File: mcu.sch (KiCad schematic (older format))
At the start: 61 parts, among them J10 JTAG, J2 SPI1, J3 uSD, J4 I2C1, J5 serial1, J6 serial2, J7 touch interface, J8 LCD 4.3, J9 EXT_IOS, SW1 reset, U3 AT25SF641, U5 STM32F750Z8, U6 MP3302DJ-LF-P, U7 ESP32-WROOM-32, Y1 25 MHz, Y2 32.768 kHz

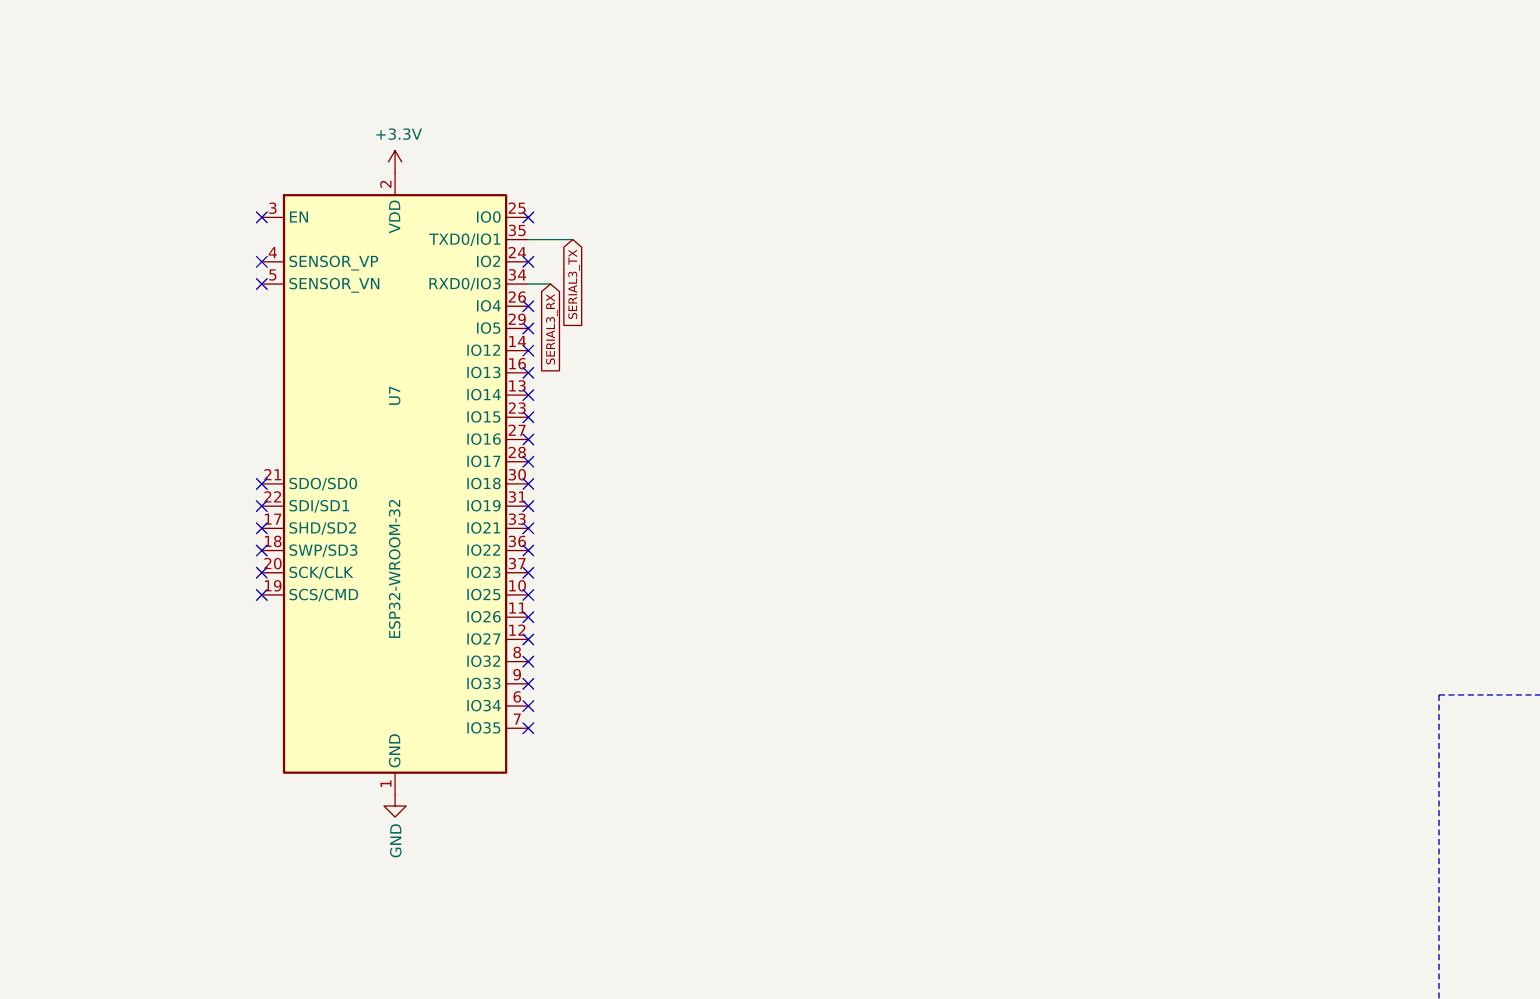
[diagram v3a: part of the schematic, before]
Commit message: add esp32 headers
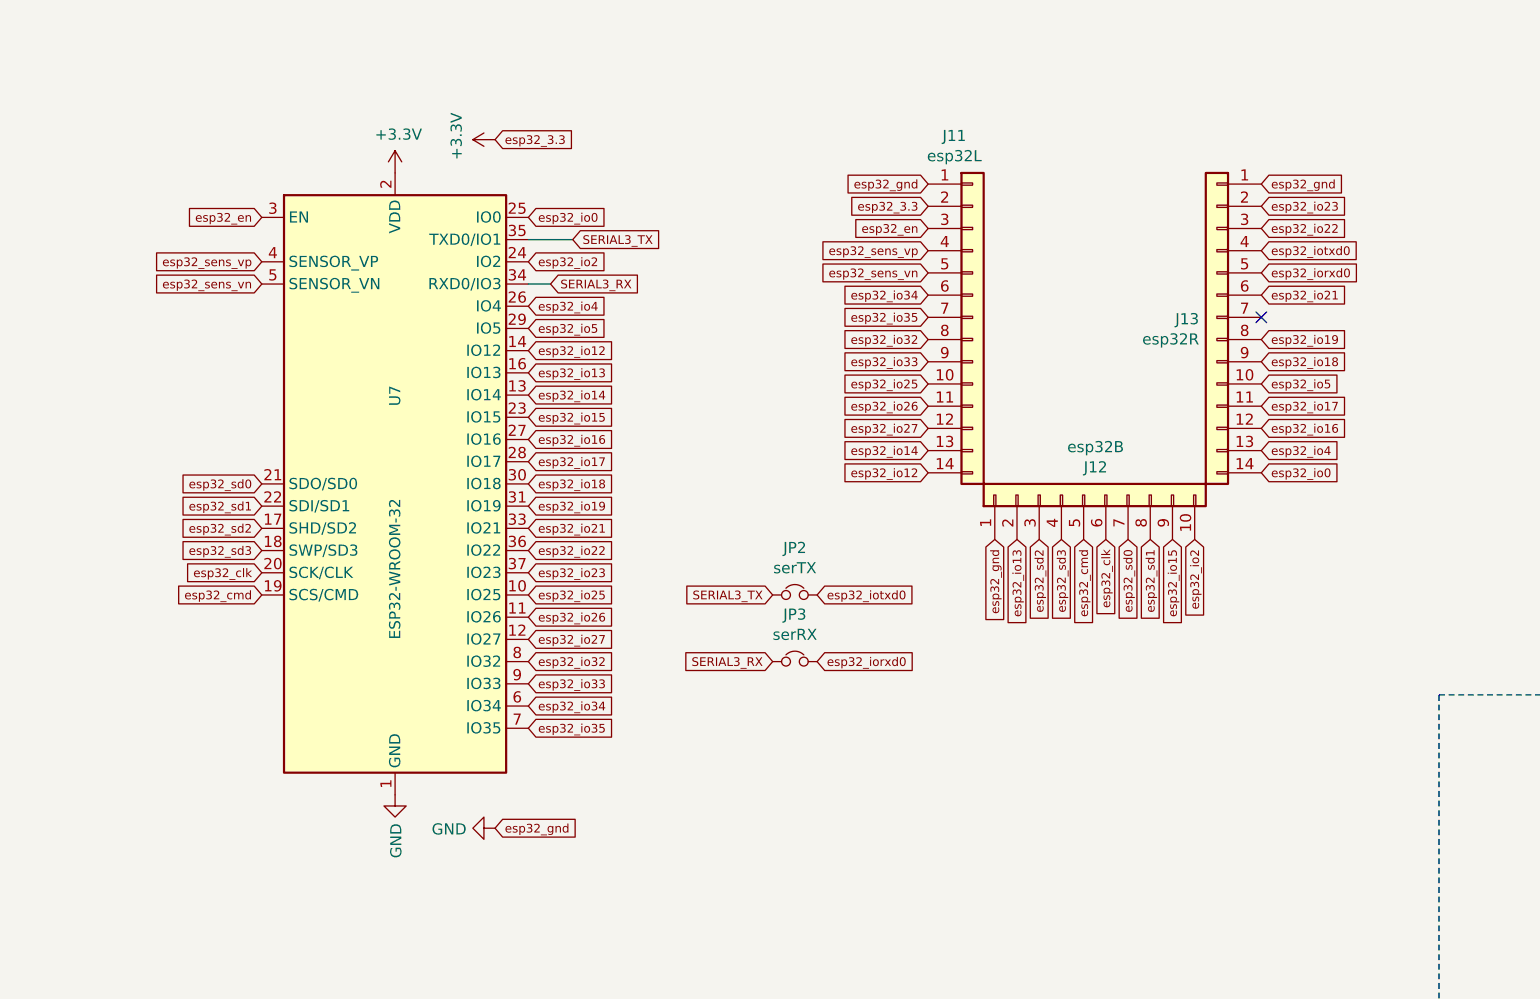
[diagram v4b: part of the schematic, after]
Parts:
- added J11: esp32L, symbol Connector_Generic:Conn_01x14
- added J12: esp32B, symbol Connector_Generic:Conn_01x10
- added J13: esp32R, symbol Connector_Generic:Conn_01x14
- added JP2: serTX, symbol Device:Jumper_NC_Small
- added JP3: serRX, symbol Device:Jumper_NC_Small
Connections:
- net +3V3: now also J11.2 (Pin_2)
- net GND: now also J11.1 (Pin_1), J12.1 (Pin_1), J13.1 (Pin_1)
- net SERIAL3_RX: now also JP3.1
- net SERIAL3_TX: now also JP2.1
- net esp32_io25: now reaches U7.10 (IO25)
- net esp32_io25: now also J11.10 (Pin_10)
- net esp32_io26: now reaches U7.11 (IO26)
- net esp32_io26: now also J11.11 (Pin_11)
- net esp32_io27: now reaches U7.12 (IO27)
- net esp32_io27: now also J11.12 (Pin_12)
- net esp32_io14: now reaches U7.13 (IO14)
- net esp32_io14: now also J11.13 (Pin_13)
- net esp32_io12: now reaches U7.14 (IO12)
- net esp32_io12: now also J11.14 (Pin_14)
- net esp32_io13: now reaches U7.16 (IO13)
- net esp32_io13: now also J12.2 (Pin_2)
- net esp32_sd2: now reaches U7.17 (SHD/SD2)
- net esp32_sd2: now also J12.3 (Pin_3)
- net esp32_sd3: now reaches U7.18 (SWP/SD3)
- net esp32_sd3: now also J12.4 (Pin_4)
- net esp32_cmd: now reaches U7.19 (SCS/CMD)
- net esp32_cmd: now also J12.5 (Pin_5)
- net esp32_clk: now reaches U7.20 (SCK/CLK)
- net esp32_clk: now also J12.6 (Pin_6)
- net esp32_sd0: now reaches U7.21 (SDO/SD0)
- net esp32_sd0: now also J12.7 (Pin_7)
- net esp32_sd1: now reaches U7.22 (SDI/SD1)
- net esp32_sd1: now also J12.8 (Pin_8)
- net esp32_io15: now reaches U7.23 (IO15)
- net esp32_io15: now also J12.9 (Pin_9)
- net esp32_io2: now reaches U7.24 (IO2)
- net esp32_io2: now also J12.10 (Pin_10)
- net esp32_io0: now reaches U7.25 (IO0)
- net esp32_io0: now also J13.14 (Pin_14)
- net esp32_io4: now reaches U7.26 (IO4)
- net esp32_io4: now also J13.13 (Pin_13)
- net esp32_io16: now reaches U7.27 (IO16)
- net esp32_io16: now also J13.12 (Pin_12)
- net esp32_io17: now reaches U7.28 (IO17)
- net esp32_io17: now also J13.11 (Pin_11)
- net esp32_io5: now reaches U7.29 (IO5)
- net esp32_io5: now also J13.10 (Pin_10)
- net esp32_en: now reaches U7.3 (EN)
- net esp32_en: now also J11.3 (Pin_3)
- net esp32_io18: now reaches U7.30 (IO18)
- net esp32_io18: now also J13.9 (Pin_9)
- net esp32_io19: now reaches U7.31 (IO19)
- net esp32_io19: now also J13.8 (Pin_8)
- net esp32_io21: now reaches U7.33 (IO21)
- net esp32_io21: now also J13.6 (Pin_6)
- net esp32_io22: now reaches U7.36 (IO22)
- net esp32_io22: now also J13.3 (Pin_3)
- net esp32_io23: now reaches U7.37 (IO23)
- net esp32_io23: now also J13.2 (Pin_2)
- net esp32_sens_vp: now reaches U7.4 (SENSOR_VP)
- net esp32_sens_vp: now also J11.4 (Pin_4)
- net esp32_sens_vn: now reaches U7.5 (SENSOR_VN)
- net esp32_sens_vn: now also J11.5 (Pin_5)
- net esp32_io34: now reaches U7.6 (IO34)
- net esp32_io34: now also J11.6 (Pin_6)
- net esp32_io35: now reaches U7.7 (IO35)
- net esp32_io35: now also J11.7 (Pin_7)
- net esp32_io32: now reaches U7.8 (IO32)
- net esp32_io32: now also J11.8 (Pin_8)
- net esp32_io33: now reaches U7.9 (IO33)
- net esp32_io33: now also J11.9 (Pin_9)
- new net esp32_iorxd0: J13.5 (Pin_5), JP3.2
- new net esp32_iotxd0: J13.4 (Pin_4), JP2.2
- no-connect marks 45 -> 15

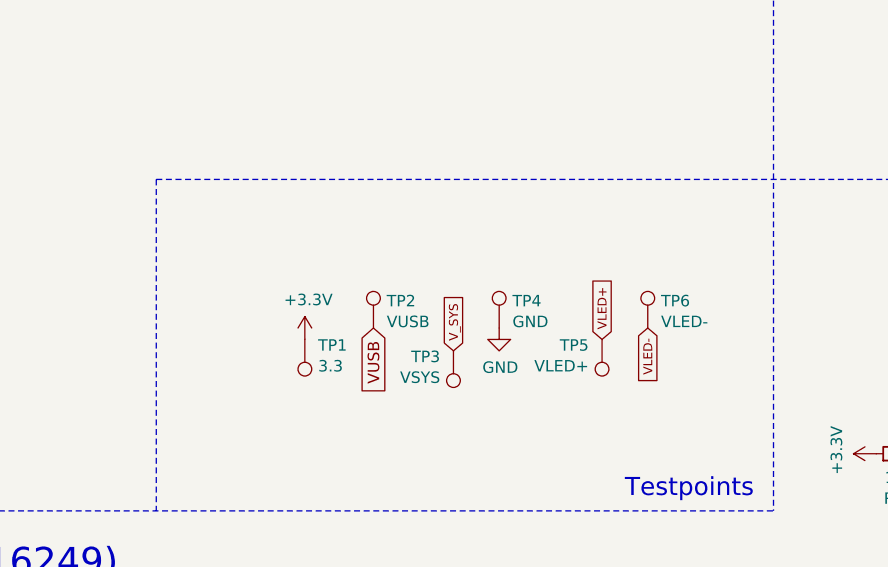
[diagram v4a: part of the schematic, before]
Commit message: Add TPs
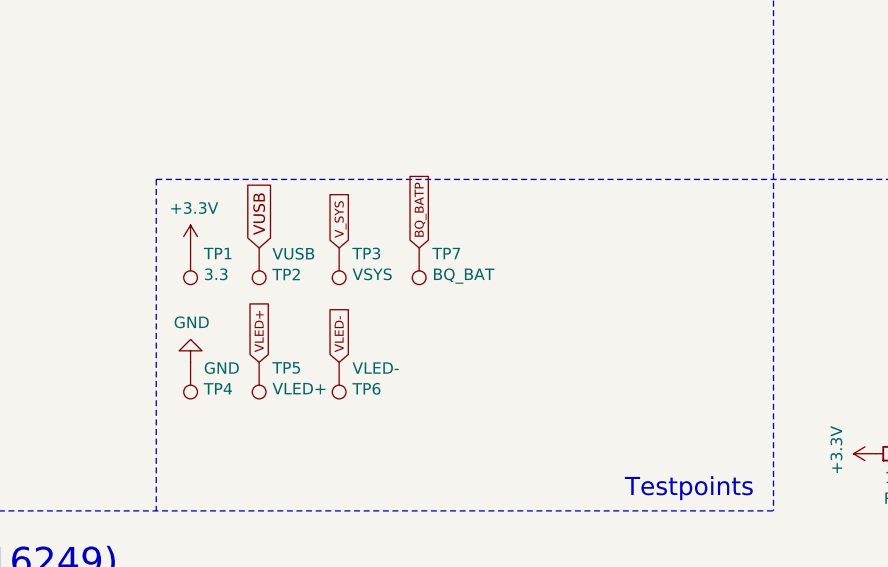
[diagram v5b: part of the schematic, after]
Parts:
- added TP7: BQ_BAT, symbol Connector:TestPoint
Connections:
- new net BQ_BATP: TP7.1
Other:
- moved on the sheet: TP1, TP2, TP3, TP4, TP5, TP6
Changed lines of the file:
@@
 L Connector:TestPoint TP1
 U 1 1 60C6D521
-P 7550 4250
-F 0 "TP1" H 7492 4276 50  0000 R CNN
-F 1 "3.3" H 7492 4367 50  0000 R CNN
-F 2 "" H 7750 4250 50  0001 C CNN
-F 3 "~" H 7750 4250 50  0001 C CNN
-	1    7550 4250
+P 7050 3850
+F 0 "TP1" H 6992 3876 50  0000 R CNN
+F 1 "3.3" H 6992 3967 50  0000 R CNN
+F 2 "" H 7250 3850 50  0001 C CNN
+F 3 "~" H 7250 3850 50  0001 C CNN
+	1    7050 3850
 	-1   0    0    1
 $EndComp
@@
 L Connector:TestPoint TP2
 U 1 1 60C6DC35
-P 7850 4200
-F 0 "TP2" H 7908 4318 50  0000 L CNN
-F 1 "VUSB" H 7908 4227 50  0000 L CNN
-F 2 "" H 8050 4200 50  0001 C CNN
-F 3 "~" H 8050 4200 50  0001 C CNN
-	1    7850 4200
-	1    0    0    -1
-$EndComp
-Text GLabel 7850 4200 3    50   Input ~ 0
+P 7350 3850
+F 0 "TP2" H 7408 3968 50  0000 L CNN
+F 1 "VUSB" H 7408 3877 50  0000 L CNN
+F 2 "" H 7550 3850 50  0001 C CNN
+F 3 "~" H 7550 3850 50  0001 C CNN
+	1    7350 3850
+	1    0    0    1
+$EndComp
+Text GLabel 7350 3850 1    50   Input ~ 0
 VUSB
 $Comp
 L Connector:TestPoint TP3
 U 1 1 60C6EE25
-P 8200 4300
-F 0 "TP3" H 8142 4326 50  0000 R CNN
-F 1 "VSYS" H 8142 4417 50  0000 R CNN
-F 2 "" H 8400 4300 50  0001 C CNN
-F 3 "~" H 8400 4300 50  0001 C CNN
-	1    8200 4300
-	1    0    0    1
-$EndComp
-Text GLabel 8200 4300 1    39   Input ~ 0
+P 7700 3850
+F 0 "TP3" H 7642 3876 50  0000 R CNN
+F 1 "VSYS" H 7642 3967 50  0000 R CNN
+F 2 "" H 7900 3850 50  0001 C CNN
+F 3 "~" H 7900 3850 50  0001 C CNN
+	1    7700 3850
+	-1   0    0    1
+$EndComp
+Text GLabel 7700 3850 1    39   Input ~ 0
 V_SYS
 $Comp
 L power:+3.3V #PWR08
 U 1 1 60C70150
-P 7550 4250
-F 0 "#PWR08" H 7550 4100 50  0001 C CNN
-F 1 "+3.3V" H 7565 4423 50  0000 C CNN
-F 2 "" H 7550 4250 50  0001 C CNN
-F 3 "" H 7550 4250 50  0001 C CNN
-	1    7550 4250
+P 7050 3850
+F 0 "#PWR08" H 7050 3700 50  0001 C CNN
+F 1 "+3.3V" H 7065 4023 50  0000 C CNN
+F 2 "" H 7050 3850 50  0001 C CNN
+F 3 "" H 7050 3850 50  0001 C CNN
+	1    7050 3850
 	1    0    0    -1
 $EndComp
@@
 L Connector:TestPoint TP4
 U 1 1 60CDAE0F
-P 8400 4200
-F 0 "TP4" H 8458 4318 50  0000 L CNN
-F 1 "GND" H 8458 4227 50  0000 L CNN
-F 2 "" H 8600 4200 50  0001 C CNN
-F 3 "~" H 8600 4200 50  0001 C CNN
-	1    8400 4200
-	1    0    0    -1
+P 7050 4350
+F 0 "TP4" H 7108 4468 50  0000 L CNN
+F 1 "GND" H 7108 4377 50  0000 L CNN
+F 2 "" H 7250 4350 50  0001 C CNN
+F 3 "~" H 7250 4350 50  0001 C CNN
+	1    7050 4350
+	1    0    0    1
 $EndComp
 $Comp
 L power:GND #PWR010
 U 1 1 60CDB10D
-P 8400 4200
-F 0 "#PWR010" H 8400 3950 50  0001 C CNN
-F 1 "GND" H 8405 4027 50  0000 C CNN
-F 2 "" H 8400 4200 50  0001 C CNN
-F 3 "" H 8400 4200 50  0001 C CNN
-	1    8400 4200
-	1    0    0    -1
+P 7050 4350
+F 0 "#PWR010" H 7050 4100 50  0001 C CNN
+F 1 "GND" H 7055 4177 50  0000 C CNN
+F 2 "" H 7050 4350 50  0001 C CNN
+F 3 "" H 7050 4350 50  0001 C CNN
+	1    7050 4350
+	1    0    0    1
 $EndComp
 Text Notes 8950 4950 0    79   ~ 0
@@
 L Connector:TestPoint TP6
 U 1 1 60CE0C95
-P 9050 4200
-F 0 "TP6" H 9108 4318 50  0000 L CNN
-F 1 "VLED-" H 9108 4227 50  0000 L CNN
-F 2 "" H 9250 4200 50  0001 C CNN
-F 3 "~" H 9250 4200 50  0001 C CNN
-	1    9050 4200
-	1    0    0    -1
+P 7700 4350
+F 0 "TP6" H 7758 4468 50  0000 L CNN
+F 1 "VLED-" H 7758 4377 50  0000 L CNN
+F 2 "" H 7900 4350 50  0001 C CNN
+F 3 "~" H 7900 4350 50  0001 C CNN
+	1    7700 4350
+	1    0    0    1
 $EndComp
 $Comp
 L Connector:TestPoint TP5
 U 1 1 60CE10AB
-P 8850 4250
-F 0 "TP5" H 8792 4276 50  0000 R CNN
-F 1 "VLED+" H 8792 4367 50  0000 R CNN
-F 2 "" H 9050 4250 50  0001 C CNN
-F 3 "~" H 9050 4250 50  0001 C CNN
-	1    8850 4250
-	1    0    0    1
-$EndComp
-Text GLabel 8850 4250 1    39   Input ~ 0
+P 7350 4350
+F 0 "TP5" H 7292 4376 50  0000 R CNN
+F 1 "VLED+" H 7292 4467 50  0000 R CNN
+F 2 "" H 7550 4350 50  0001 C CNN
+F 3 "~" H 7550 4350 50  0001 C CNN
+	1    7350 4350
+	-1   0    0    1
+$EndComp
+Text GLabel 7350 4350 1    39   Input ~ 0
 VLED+
-Text GLabel 9050 4200 3    39   Input ~ 0
+Text GLabel 7700 4350 1    39   Input ~ 0
 VLED-
 Wire Notes Line
@@
 Text GLabel 1600 3100 0    39   Input ~ 0
 esp32_cmd
+Text GLabel 8050 3850 1    39   Input ~ 0
+BQ_BATP
+$Comp
+L Connector:TestPoint TP7
+U 1 1 60FE1681
+P 8050 3850
+F 0 "TP7" H 7992 3876 50  0000 R CNN
+F 1 "BQ_BAT" H 7992 3967 50  0000 R CNN
+F 2 "" H 8250 3850 50  0001 C CNN
+F 3 "~" H 8250 3850 50  0001 C CNN
+	1    8050 3850
+	-1   0    0    1
+$EndComp
 $EndSCHEMATC

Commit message: it is
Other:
- note added: "TODO to validate:\n- BOOT0 behavior\n- WAKEUP through ON behavior\n- RESET\n- caps for stm32 25MHz xtal"
- note removed: "TODO to validate:\n- BOOT0 behavior\n- WAKEUP through ON behavior\n- RESET\n- caps for stm32 25MHz xtal\n- if usb host, VUSB isn't powered"
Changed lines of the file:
@@
 BOOT0
 Text Notes 600  11100 0    98   ~ 0
-TODO to validate:\n- BOOT0 behavior\n- WAKEUP through ON behavior\n- RESET\n- caps for stm32 25MHz xtal\n- if usb host, VUSB isn't powered
+TODO to validate:\n- BOOT0 behavior\n- WAKEUP through ON behavior\n- RESET\n- caps for stm32 25MHz xtal
 Text GLabel 4800 9350 0    50   Input ~ 0
 KB_ROW_11

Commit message: switch to right xtals
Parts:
- removed C30: 10pF, symbol Device:C_Small
- removed Y1: 25 MHz, symbol Device:Crystal
- added R25: 10k, symbol Device:R_Small
- added R26: 100, symbol Device:R_Small
- added U8: ASDMB-25.000MHZ-LC-T, Oscillator:Oscillator_SMD_Abracon_ASDMB-4Pin_2.5x2.0mm, symbol Oscillator:ASDMB-xxxMHz
- C29: value 10pF -> 100nF
- Y2: mouser (none) -> 815-ABS0716632.768KT
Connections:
- net +3V3: now also C29.1, R25.1, U8.4 (VDD)
- net GND: now also C29.2, U8.2 (GND); no longer C29.1
- net OSC_IN: no longer names the net of U5.23 (PH0)
- net OSC_IN: now also R26.1; no longer C29.2
- net OSC_OUT: no longer names the net of U5.24 (PH1)
- new net: R25.2, U8.1 (Standby)
- new net OSC_25M: R26.2, U8.3 (Out)
- no-connect marks 15 -> 16
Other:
- note added: "ABS07-166-32.768KHZ-T"
- note added: "TODO to validate:\n- BOOT0 behavior\n- WAKEUP through ON behavior\n- RESET"
- note removed: "TODO to validate:\n- BOOT0 behavior\n- WAKEUP through ON behavior\n- RESET\n- caps for stm32 25MHz xtal"
- note removed: "xtal with\nintegrated\ncaps"
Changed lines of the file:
@@
 $EndDescr
-$Comp
-L Device:Crystal Y1
-U 1 1 5F7C8337
-P 12000 3600
-F 0 "Y1" H 12000 3868 50  0000 C CNN
-F 1 "25 MHz" H 12000 3777 50  0000 C CNN
-F 2 "" H 12000 3600 50  0001 C CNN
-F 3 "~" H 12000 3600 50  0001 C CNN
-	1    12000 3600
-	0    1    1    0
-$EndComp
 $Comp
 L Device:Crystal Y2
@@
 F 2 "" H 15950 7000 50  0001 C CNN
 F 3 "~" H 15950 7000 50  0001 C CNN
+F 4 "815-ABS0716632.768KT" H 15950 7000 50  0001 C CNN "mouser"
 	1    15950 7000
 	0    -1   -1   0
@@
 Text Label 15100 7050 0    39   ~ 0
 OSC32_OUT
-Text Notes 15650 6700 0    39   ~ 0
-xtal with\nintegrated\ncaps
-Text Label 12450 3550 0    39   ~ 0
-OSC_IN
-Text Label 12450 3650 0    39   ~ 0
-OSC_OUT
-Wire Wire Line
-	12750 3650 12300 3650
-Wire Wire Line
-	12300 3650 12300 3800
-Wire Wire Line
-	12300 3800 12000 3800
-Wire Wire Line
-	12000 3800 12000 3750
-Wire Wire Line
-	12000 3450 12000 3400
-Wire Wire Line
-	12000 3400 12300 3400
-Wire Wire Line
-	12300 3400 12300 3550
-Wire Wire Line
-	12300 3550 12750 3550
 Text GLabel 14500 1950 1    50   Input ~ 0
 VUSB
@@
 BOOT0
 Text Notes 600  11100 0    98   ~ 0
-TODO to validate:\n- BOOT0 behavior\n- WAKEUP through ON behavior\n- RESET\n- caps for stm32 25MHz xtal
+TODO to validate:\n- BOOT0 behavior\n- WAKEUP through ON behavior\n- RESET
 Text GLabel 4800 9350 0    50   Input ~ 0
 KB_ROW_11
@@
 Wire Wire Line
 	10600 1850 10900 1850
-$Comp
-L Device:C_Small C29
-U 1 1 602A0B0B
-P 11900 3400
-F 0 "C29" V 12129 3400 50  0000 C CNN
-F 1 "10pF" V 12038 3400 50  0000 C CNN
-F 2 "" H 11900 3400 50  0001 C CNN
-F 3 "~" H 11900 3400 50  0001 C CNN
-	1    11900 3400
-	0    -1   -1   0
-$EndComp
-Connection ~ 12000 3400
-$Comp
-L Device:C_Small C30
-U 1 1 602A1326
-P 11900 3800
-F 0 "C30" V 11700 3800 50  0000 C CNN
-F 1 "10pF" V 11800 3800 50  0000 C CNN
-F 2 "" H 11900 3800 50  0001 C CNN
-F 3 "~" H 11900 3800 50  0001 C CNN
-	1    11900 3800
-	0    -1   -1   0
-$EndComp
-Connection ~ 12000 3800
-$Comp
-L power:GND #PWR0140
-U 1 1 602A1994
-P 11800 3400
-F 0 "#PWR0140" H 11800 3150 50  0001 C CNN
-F 1 "GND" H 11805 3227 50  0000 C CNN
-F 2 "" H 11800 3400 50  0001 C CNN
-F 3 "" H 11800 3400 50  0001 C CNN
-	1    11800 3400
-	0    1    1    0
-$EndComp
-$Comp
-L power:GND #PWR0141
-U 1 1 602A2015
-P 11800 3800
-F 0 "#PWR0141" H 11800 3550 50  0001 C CNN
-F 1 "GND" H 11805 3627 50  0000 C CNN
-F 2 "" H 11800 3800 50  0001 C CNN
-F 3 "" H 11800 3800 50  0001 C CNN
-	1    11800 3800
-	0    1    1    0
-$EndComp
 Text Notes 11550 4200 0    39   ~ 0
 validate caps against\nchoosen xtal
@@
 	-1   0    0    1
 $EndComp
+Text Notes 15650 6700 0    39   ~ 0
+ABS07-166-32.768KHZ-T
+$Comp
+L Oscillator:ASDMB-xxxMHz U8
+U 1 1 60FEB22A
+P 10600 2950
+F 0 "U8" H 11044 2996 50  0000 L CNN
+F 1 "ASDMB-25.000MHZ-LC-T" H 10100 2500 50  0000 L CNN
+F 2 "Oscillator:Oscillator_SMD_Abracon_ASDMB-4Pin_2.5x2.0mm" H 10600 2950 50  0001 C CNN
+F 3 "https://abracon.com/Oscillators/ASDMB.pdf" H 10900 3400 50  0001 C CNN
+	1    10600 2950
+	1    0    0    -1
+$EndComp
+$Comp
+L Device:R_Small R25
+U 1 1 60FEC7BE
+P 10000 2950
+F 0 "R25" V 10196 2950 50  0000 C CNN
+F 1 "10k" V 10105 2950 50  0000 C CNN
+F 2 "" H 10000 2950 50  0001 C CNN
+F 3 "~" H 10000 2950 50  0001 C CNN
+	1    10000 2950
+	0    -1   -1   0
+$EndComp
+$Comp
+L Device:C_Small C29
+U 1 1 60FED86D
+P 9850 3150
+F 0 "C29" H 9942 3196 50  0000 L CNN
+F 1 "100nF" H 9942 3105 50  0000 L CNN
+F 2 "" H 9850 3150 50  0001 C CNN
+F 3 "~" H 9850 3150 50  0001 C CNN
+	1    9850 3150
+	1    0    0    -1
+$EndComp
+$Comp
+L power:+3.3V #PWR045
+U 1 1 60FEF86B
+P 9850 2650
+F 0 "#PWR045" H 9850 2500 50  0001 C CNN
+F 1 "+3.3V" H 9865 2823 50  0000 C CNN
+F 2 "" H 9850 2650 50  0001 C CNN
+F 3 "" H 9850 2650 50  0001 C CNN
+	1    9850 2650
+	1    0    0    -1
+$EndComp
+$Comp
+L power:GND #PWR046
+U 1 1 60FEFF10
+P 9850 3250
+F 0 "#PWR046" H 9850 3000 50  0001 C CNN
+F 1 "GND" H 9855 3077 50  0000 C CNN
+F 2 "" H 9850 3250 50  0001 C CNN
+F 3 "" H 9850 3250 50  0001 C CNN
+	1    9850 3250
+	1    0    0    -1
+$EndComp
+Wire Wire Line
+	10700 3250 9850 3250
+Connection ~ 9850 3250
+Wire Wire Line
+	9850 3050 9850 2950
+Wire Wire Line
+	9900 2950 9850 2950
+Connection ~ 9850 2950
+Wire Wire Line
+	9850 2950 9850 2650
+Wire Wire Line
+	10700 2650 9850 2650
+Connection ~ 9850 2650
+Wire Wire Line
+	10100 2950 10200 2950
+$Comp
+L Device:R_Small R26
+U 1 1 61011743
+P 12200 3550
+F 0 "R26" V 12004 3550 50  0000 C CNN
+F 1 "100" V 12095 3550 50  0000 C CNN
+F 2 "" H 12200 3550 50  0001 C CNN
+F 3 "~" H 12200 3550 50  0001 C CNN
+	1    12200 3550
+	0    1    1    0
+$EndComp
+Wire Wire Line
+	12300 3550 12750 3550
+Wire Wire Line
+	12100 3550 11650 3550
+Wire Wire Line
+	11650 3550 11650 2950
+Wire Wire Line
+	11650 2950 11000 2950
+Text Label 11250 2950 0    39   ~ 0
+OSC_25M
+NoConn ~ 12750 3650
 $EndSCHEMATC
